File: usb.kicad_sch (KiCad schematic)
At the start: 24 parts, among them J4 CONN_02X03, U1 LFE5U-85F-6BG381C, U6 FT231XS, Y1 FNETHE025

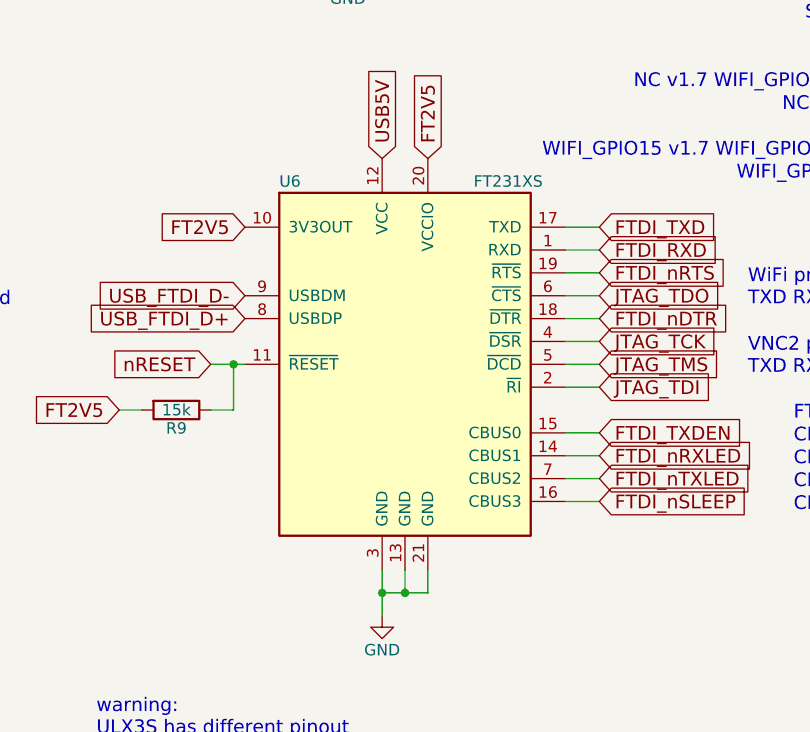
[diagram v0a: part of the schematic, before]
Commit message: fix footprint/symbol for ft231- need to re-work routing
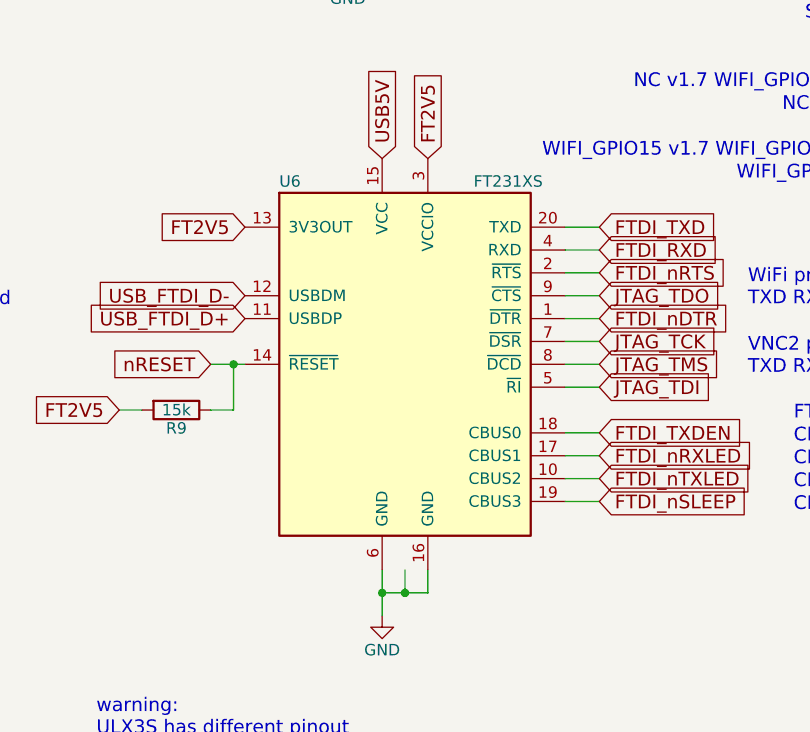
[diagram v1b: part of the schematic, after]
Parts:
- U6: symbol ftdi:FT231XQ -> ftdi:FT231XS
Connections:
- net FT2V5: now also U6.13 (3V3OUT), U6.3 (VCCIO); no longer U6.10 (3V3OUT), U6.20 (VCCIO)
- net FTDI_RXD: now also U6.4 (RXD); no longer U6.1 (RXD)
- net FTDI_TXD: now also U6.20 (TXD); no longer U6.17 (TXD)
- net FTDI_TXDEN: now also U6.18 (CBUS0); no longer U6.15 (CBUS0)
- net FTDI_nDTR: now also U6.1 (~{DTR}); no longer U6.18 (~{DTR})
- net FTDI_nRTS: now also U6.2 (~{RTS}); no longer U6.19 (~{RTS})
- net FTDI_nRXLED: now also U6.17 (CBUS1); no longer U6.14 (CBUS1)
- net FTDI_nSLEEP: now also U6.19 (CBUS3); no longer U6.16 (CBUS3)
- net FTDI_nTXLED: now also U6.10 (CBUS2); no longer U6.7 (CBUS2)
- net GND: now also U6.16 (GND), U6.6 (GND); no longer U6.13 (GND), U6.21 (GND), U6.3 (GND)
- net JTAG_TCK: now also U6.7 (~{DSR}); no longer U6.4 (~{DSR})
- net JTAG_TDI: now also U6.5 (~{RI}); no longer U6.2 (~{RI})
- net JTAG_TDO: now also U6.9 (~{CTS}); no longer U6.6 (~{CTS})
- net JTAG_TMS: now also U6.8 (~{DCD}); no longer U6.5 (~{DCD})
- net USB5V: now also U6.15 (VCC); no longer U6.12 (VCC)
- net USB_FTDI_D+: now also U6.11 (USBDP); no longer U6.8 (USBDP)
- net USB_FTDI_D-: now also U6.12 (USBDM); no longer U6.9 (USBDM)
- net nRESET: now also U6.14 (~{RESET}); no longer U6.11 (~{RESET})
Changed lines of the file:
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@@
 	)
 	(symbol
-		(lib_id "ftdi:FT231XQ")
+		(lib_id "ftdi:FT231XS")
 		(at 144.78 86.36 0)
 		(unit 1)
@@
 			)
 		)
-		(property "Datasheet" "https://ftdichip.com/wp-content/uploads/2021/10/DS_FT231X.pdf"
-			(at 144.78 86.36 0)
-			(hide yes)
-			(show_name no)
-			(do_not_autoplace no)
-			(effects
-				(font
-					(size 1.27 1.27)
-				)
-			)
-		)
-		(property "Description" ""
-			(at 144.78 86.36 0)
+		(property "Datasheet" "http://www.ftdichip.com/Products/ICs/FT231X.html"
+			(at 144.78 86.36 0)
+			(hide yes)
+			(show_name no)
+			(do_not_autoplace no)
+			(effects
+				(font
+					(size 1.27 1.27)
+				)
+			)
+		)
+		(property "Description" "Full Speed USB to Full Handshake UART, SSOP-20"
+			(at 144.78 86.36 0)
+			(hide yes)
 			(show_name no)
 			(do_not_autoplace no)
@@
 		(pin "20"
 		)
-		(pin "21"
-		)
 		(pin "17"

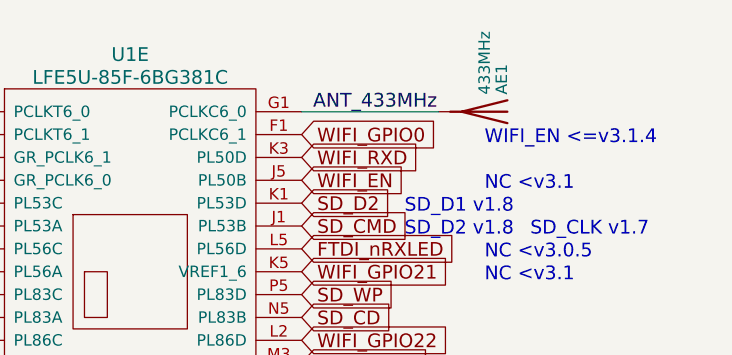
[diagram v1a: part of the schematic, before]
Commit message: remove 433mhz ant
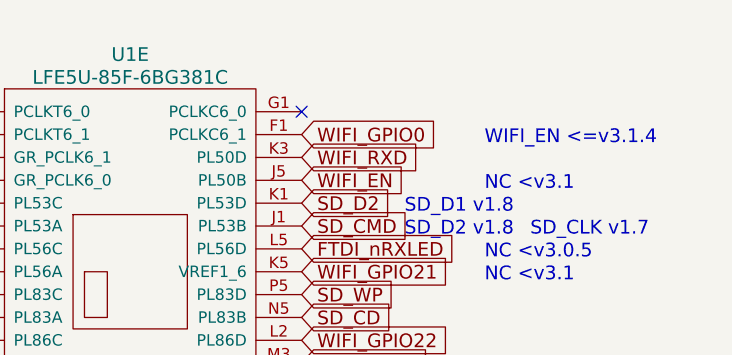
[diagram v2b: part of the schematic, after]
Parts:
- removed AE1: 433MHz, TestPoint:TestPoint_Pad_D1.0mm, symbol Device:Antenna
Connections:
- net ANT_433MHz: no longer names the net of U1.G1 (PCLKC6_0)
- no-connect marks 7 -> 8
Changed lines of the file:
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@@
 	)
 	(no_connect
+		(at 257.81 34.29)
+	)
+	(no_connect
 		(at 219.71 69.85)
 	)
@@
 	(wire
 		(pts
-			(xy 257.81 34.29) (xy 273.05 34.29)
-		)
-		(stroke
-			(width 0)
-			(type default)
-		)
-	)
-	(wire
-		(pts
 			(xy 45.72 48.26) (xy 54.61 48.26)
 		)
@@
 		)
 	)
-	(label "ANT_433MHz"
-		(at 259.08 34.29 0)
-		(effects
-			(font
-				(size 1.524 1.524)
-			)
-			(justify left bottom)
-		)
-	)
 	(label "FPD+"
 		(at 46.99 72.39 0)
@@
 					(unit 1)
 				)
-			)
-		)
-	)
-	(symbol
-		(lib_id "Device:Antenna")
-		(at 278.13 34.29 270)
-		(unit 1)
-		(body_style 1)
-		(exclude_from_sim no)
-		(in_bom no)
-		(on_board yes)
-		(in_pos_files yes)
-		(dnp no)
-		(property "Reference" "AE1"
-			(at 280.035 32.385 0)
-			(show_name no)
-			(do_not_autoplace no)
-			(effects
-				(font
-					(size 1.27 1.27)
-				)
-				(justify right)
-			)
-		)
-		(property "Value" "433MHz"
-			(at 278.13 32.385 0)
-			(show_name no)
-			(do_not_autoplace no)
-			(effects
-				(font
-					(size 1.27 1.27)
-				)
-				(justify right)
-			)
-		)
-		(property "Footprint" "TestPoint:TestPoint_Pad_D1.0mm"
-			(at 278.13 34.29 0)
-			(hide yes)
-			(show_name no)
-			(do_not_autoplace no)
-			(effects
-				(font
-					(size 1.27 1.27)
-				)
-			)
-		)
-		(property "Datasheet" ""
-			(at 278.13 34.29 0)
-			(hide yes)
-			(show_name no)
-			(do_not_autoplace no)
-			(effects
-				(font
-					(size 1.27 1.27)
-				)
-			)
-		)
-		(property "Description" ""
-			(at 278.13 34.29 0)
-			(show_name no)
-			(do_not_autoplace no)
-			(effects
-				(font
-					(size 1.27 1.27)
-				)
-			)
-		)
-		(property "Note" "Leave empty"
-			(at 278.13 34.29 0)
-			(hide yes)
-			(show_name no)
-			(do_not_autoplace no)
-			(effects
-				(font
-					(size 1.524 1.524)
-				)
-			)
-		)
-		(pin "1"
-		)
-		(instances
-			(project "ulx3s"
-				(path "/49a43414-f3c1-43b2-ad20-ac3166075f21/00000000-0000-0000-0000-000058d6bf46"
-					(reference "AE1")
-					(unit 1)
-				)

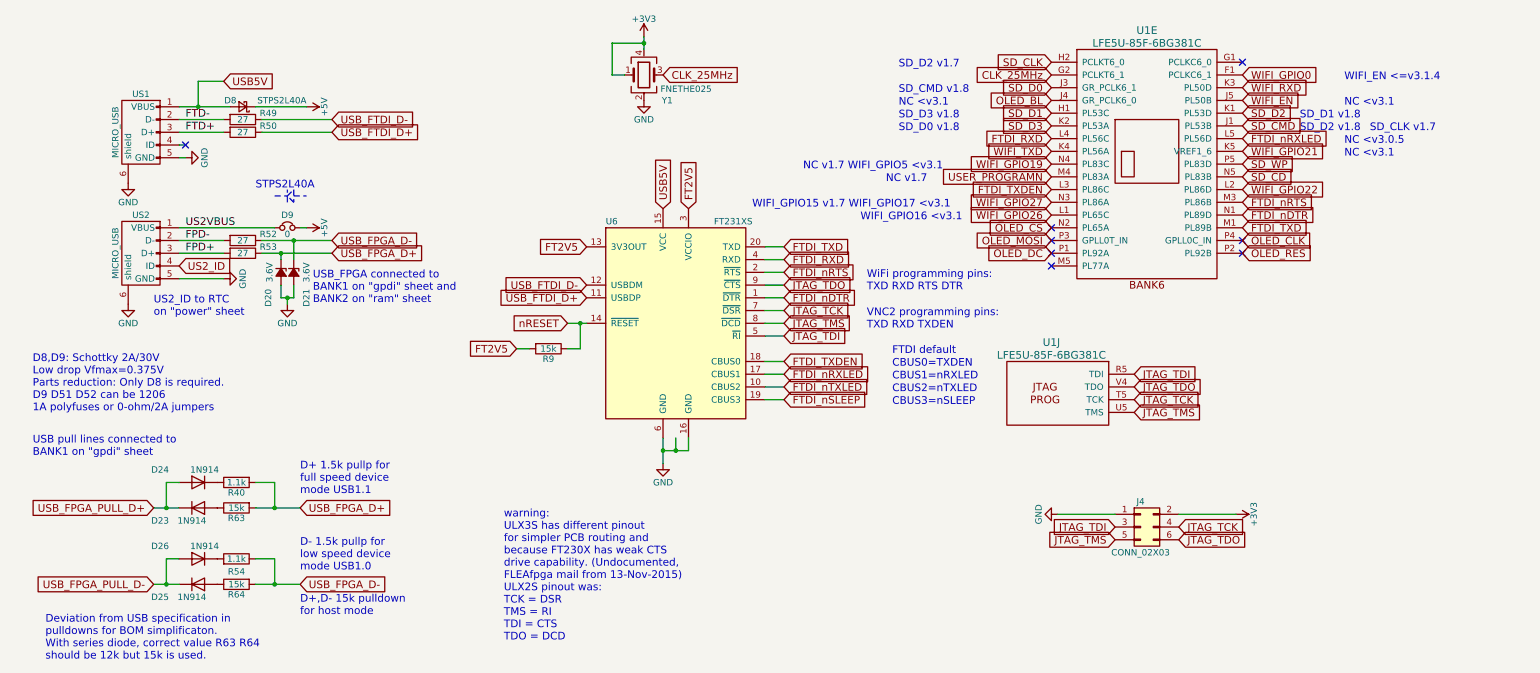
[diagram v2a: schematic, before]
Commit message: Remove 'Leave Empty' in favor of using attributes
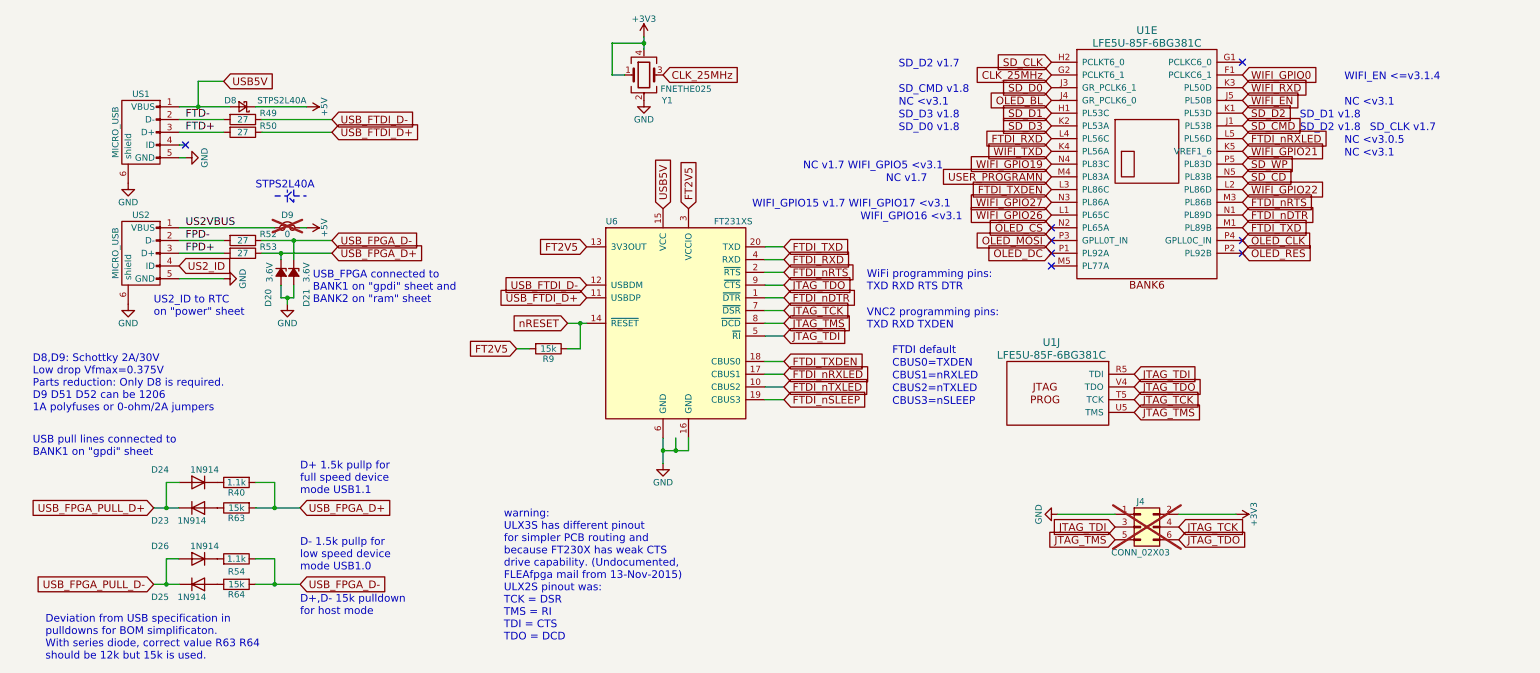
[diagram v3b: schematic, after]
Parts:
- D9, J4: Note Leave empty -> (none); now not fitted
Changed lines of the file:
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@@
 		(in_bom no)
 		(on_board yes)
-		(in_pos_files yes)
-		(dnp no)
+		(in_pos_files no)
+		(dnp yes)
 		(property "Reference" "D9"
 			(at 67.31 64.77 0)
@@
 			)
 		)
-		(property "Note" "Leave empty"
+		(property "Note" ""
 			(at 67.31 67.31 0)
 			(hide yes)
@@
 		(in_bom no)
 		(on_board yes)
-		(in_pos_files yes)
-		(dnp no)
+		(in_pos_files no)
+		(dnp yes)
 		(property "Reference" "J4"
 			(at 237.49 121.92 0)
@@
 			)
 		)
-		(property "Note" "Leave empty"
+		(property "Note" ""
 			(at 237.49 127 0)
 			(hide yes)

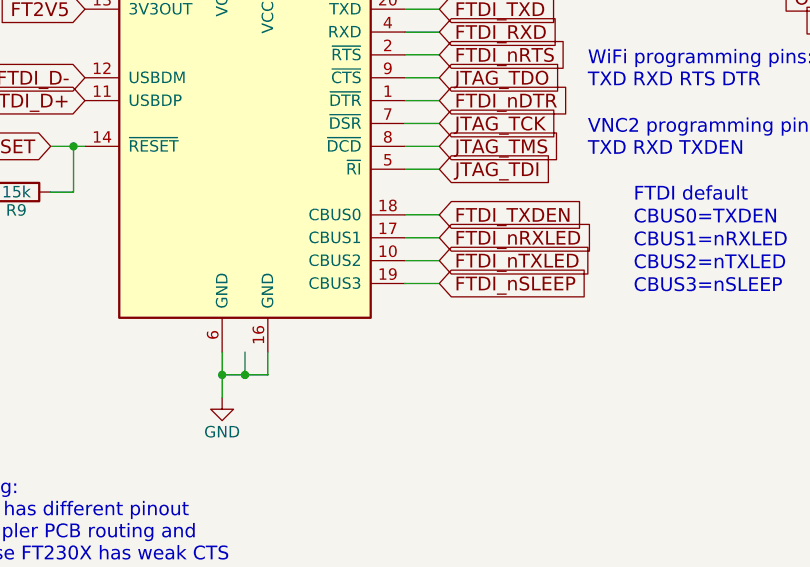
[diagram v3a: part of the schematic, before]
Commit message: remove wake up/shutdown logic
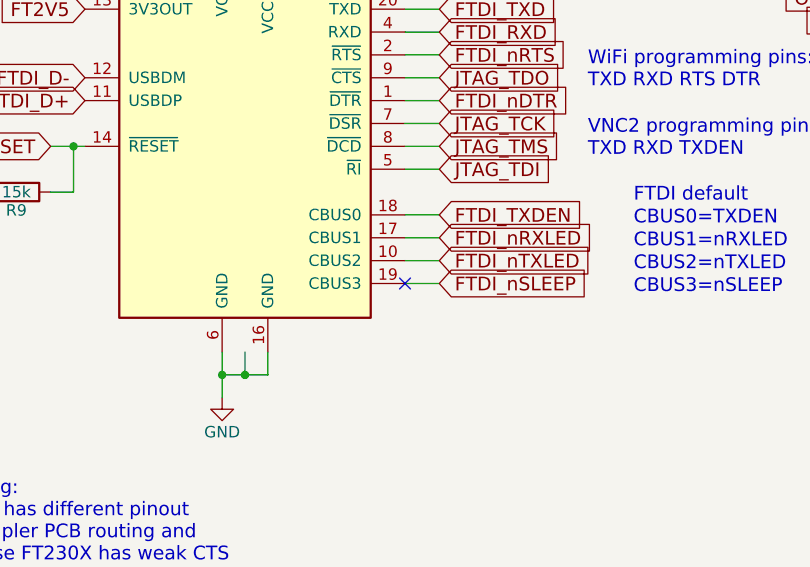
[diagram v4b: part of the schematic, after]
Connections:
- no-connect marks 8 -> 9
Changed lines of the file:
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@@
+	)
+	(no_connect
+		(at 162.56 101.6)
 	)
 	(no_connect

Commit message: update parts for 22uf/1uf. Update footprint for RP* items
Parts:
- D23, D24, D25, D26: Digikey 1N914BWSCT-ND -> 1N9148WSCT-ND

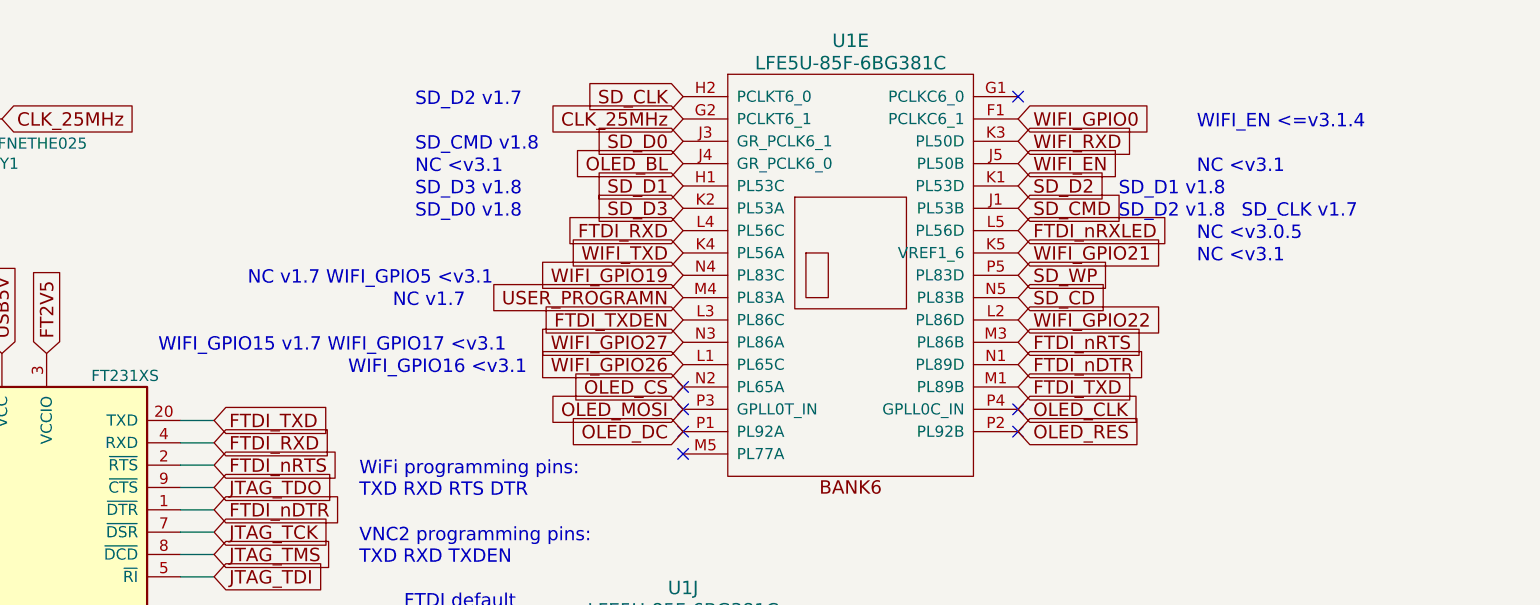
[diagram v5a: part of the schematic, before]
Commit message: reposition flash to bottom. route esp32-s3. fix drc issues
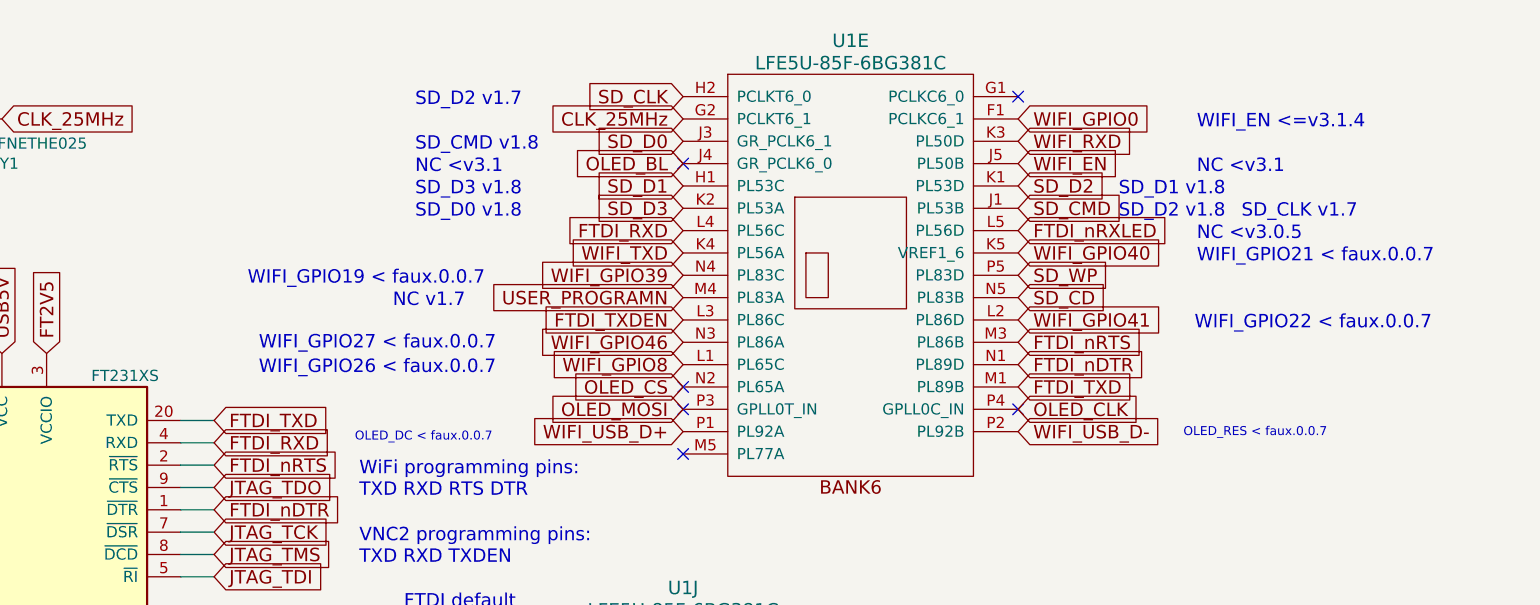
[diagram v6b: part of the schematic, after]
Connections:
- net OLED_DC renamed WIFI_USB_D+
- net OLED_RES renamed WIFI_USB_D-
- net WIFI_GPIO19 renamed WIFI_GPIO39
- net WIFI_GPIO21 renamed WIFI_GPIO40
- net WIFI_GPIO22 renamed WIFI_GPIO41
- net WIFI_GPIO26 renamed WIFI_GPIO8
- net WIFI_GPIO27 renamed WIFI_GPIO46
- no-connect marks 9 -> 8
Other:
- note added: "OLED_DC < faux.0.0.7"
- note added: "OLED_RES < faux.0.0.7"
- note added: "WIFI_GPIO19 < faux.0.0.7"
- note added: "WIFI_GPIO21 < faux.0.0.7"
- note added: "WIFI_GPIO22 < faux.0.0.7"
- note added: "WIFI_GPIO26 < faux.0.0.7"
- note added: "WIFI_GPIO27 < faux.0.0.7"
- note removed: "NC v1.7 WIFI_GPIO5 <v3.1"
- note removed: "WIFI_GPIO15 v1.7 WIFI_GPIO17 <v3.1"
- note removed: "WIFI_GPIO16 <v3.1"
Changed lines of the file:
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@@
+		)
+	)
+	(text "OLED_DC < faux.0.0.7"
+		(exclude_from_sim no)
+		(at 182.372 73.66 0)
+		(effects
+			(font
+				(size 1.016 1.016)
+			)
+			(justify left bottom)
 		)
 	)
@@
 		)
 	)
+	(text "WIFI_GPIO22 < faux.0.0.7"
+		(exclude_from_sim no)
+		(at 277.876 60.96 0)
+		(effects
+			(font
+				(size 1.524 1.524)
+			)
+			(justify left bottom)
+		)
+	)
 	(text "SD_D2 v1.7"
 		(exclude_from_sim no)
@@
 		)
 	)
-	(text "WIFI_GPIO15 v1.7 WIFI_GPIO17 <v3.1"
-		(exclude_from_sim no)
-		(at 160.02 63.5 0)
+	(text "WIFI_GPIO27 < faux.0.0.7"
+		(exclude_from_sim no)
+		(at 171.45 63.246 0)
 		(effects
 			(font
@@
 		)
 	)
+	(text "OLED_RES < faux.0.0.7"
+		(exclude_from_sim no)
+		(at 276.606 73.152 0)
+		(effects
+			(font
+				(size 1.016 1.016)
+			)
+			(justify left bottom)
+		)
+	)
 	(text "CBUS2=nTXLED"
 		(exclude_from_sim no)
@@
 		)
 	)
-	(text "NC v1.7 WIFI_GPIO5 <v3.1"
+	(text "WIFI_GPIO19 < faux.0.0.7"
 		(exclude_from_sim no)
 		(at 170.18 55.88 0)
@@
 		)
 	)
-	(text "NC <v3.1"
+	(text "WIFI_GPIO21 < faux.0.0.7"
 		(exclude_from_sim no)
 		(at 278.13 53.34 0)
@@
 		)
 	)
-	(text "WIFI_GPIO16 <v3.1"
-		(exclude_from_sim no)
-		(at 181.61 66.04 0)
+	(text "WIFI_GPIO26 < faux.0.0.7"
+		(exclude_from_sim no)
+		(at 171.45 66.04 0)
 		(effects
 			(font
@@
 	)
 	(no_connect
-		(at 219.71 72.39)
-	)
-	(no_connect
 		(at 257.81 69.85)
 	)
@@
 	)
 	(no_connect
-		(at 257.81 72.39)
+		(at 219.71 41.91)
 	)
 	(polyline
@@
 		)
 	)
-	(global_label "WIFI_GPIO21"
+	(global_label "WIFI_GPIO40"
 		(shape input)
 		(at 257.81 52.07 0)
@@
 		)
 	)
-	(global_label "WIFI_GPIO26"
+	(global_label "WIFI_GPIO8"
 		(shape input)
 		(at 219.71 64.77 180)
@@
 		)
 	)
-	(global_label "WIFI_GPIO27"
+	(global_label "WIFI_GPIO46"
 		(shape input)
 		(at 219.71 62.23 180)
@@
 		)
 	)
-	(global_label "WIFI_GPIO22"
+	(global_label "WIFI_GPIO41"
 		(shape input)
 		(at 257.81 59.69 0)
@@
 		)
 	)
-	(global_label "OLED_RES"
+	(global_label "WIFI_USB_D-"
 		(shape input)
 		(at 257.81 72.39 0)
@@
 		)
 	)
-	(global_label "WIFI_GPIO19"
+	(global_label "WIFI_GPIO39"
 		(shape input)
 		(at 219.71 54.61 180)
@@
 		)
 	)
-	(global_label "OLED_DC"
+	(global_label "WIFI_USB_D+"
 		(shape input)
 		(at 219.71 72.39 180)
